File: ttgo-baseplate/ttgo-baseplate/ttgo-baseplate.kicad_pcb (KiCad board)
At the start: 4 copper layers, 55.1 x 76.6 mm, 4 parts, among them J1 Conn_02x16_Odd_Even, J2 Conn_02x16_Odd_Even, J3 Conn_02x10_Odd_Even, J4 Conn_01x05

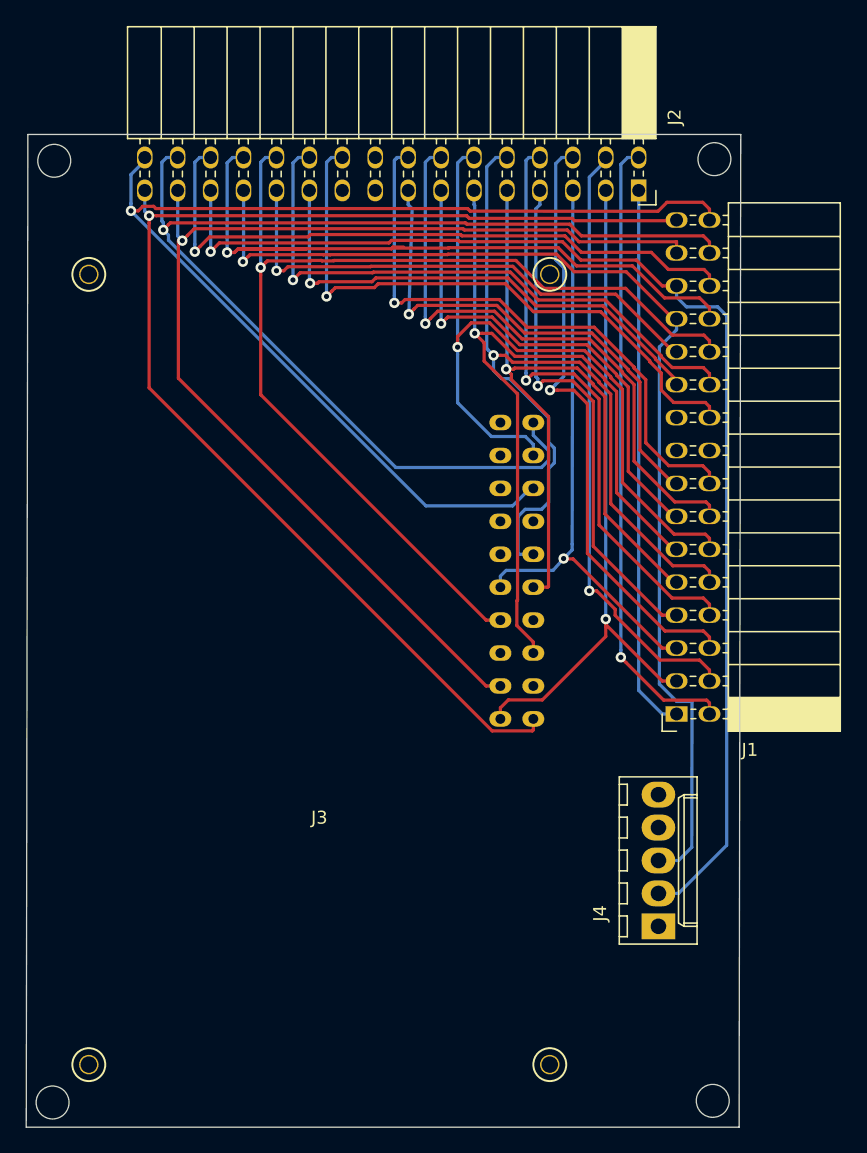
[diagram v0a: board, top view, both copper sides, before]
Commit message: texts added
new images for webpage
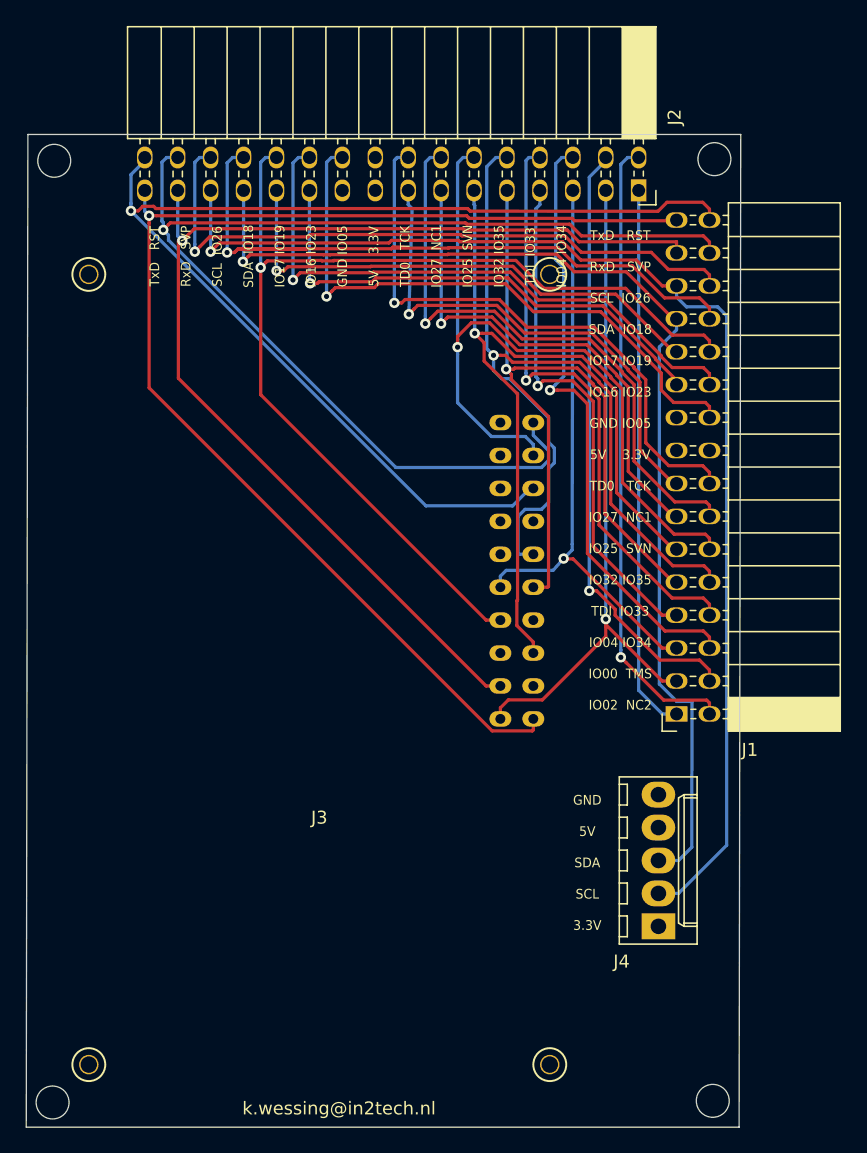
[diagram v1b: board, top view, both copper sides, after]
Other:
- board text added: "GND 5V SDA SCL 3.3V"
- board text added: "TTGO - BOARD Sensemakers - in2tech"
- board text added: "TxD RST RxD SVP SCL IO26 SDA IO18 IO17 IO19 IO16 IO23 GND IO05 5V 3.3V TD0 TCK IO27 NC1 IO25 SVN IO32 IO35 TDI IO33 IO04 IO34"
- board text added: "TxD RST RxD SVP SCL IO26 SDA IO18 IO17 IO19 IO16 IO23 GND IO05 5V 3.3V TD0 TCK IO27 NC1 IO25 SVN IO32 IO35 TDI IO33 IO04 IO34 IO00 TMS IO02 NC2"
- board text added: "k.wessing@in2tech.nl"
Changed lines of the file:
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@@
   (general
     (thickness 1.6)
-    (drawings 22)
+    (drawings 28)
     (tracks 538)
     (zones 0)
@@
     (descr "Connector Headers with Friction Lock, 22-27-2051, http://www.molex.com/pdm_docs/sd/022272021_sd.pdf")
     (tags "connector molex kk_6410 22-27-2051")
-    (fp_text reference J4 (at 1 -4.5 90) (layer F.SilkS)
+    (fp_text reference J4 (at -2.7178 -2.8448 180) (layer F.SilkS)
       (effects (font (size 1 1) (thickness 0.15)))
     )
@@
     )
   )
+  (gr_text "TTGO - BOARD\nSensemakers - in2tech" (at 138.0236 135.89) (layer B.SilkS)
+    (effects (font (size 1 1) (thickness 0.15)) (justify mirror))
+  )
+  (gr_text k.wessing@in2tech.nl (at 137.4648 142.2908) (layer B.SilkS)
+    (effects (font (size 1 1) (thickness 0.15)) (justify mirror))
+  )
+  (gr_text k.wessing@in2tech.nl (at 137.668 147.2692) (layer F.SilkS)
+    (effects (font (size 1 1) (thickness 0.15)))
+  )
+  (gr_text "GND\n\n5V\n\nSDA\n\nSCL\n\n3.3V" (at 156.8196 128.3208) (layer F.SilkS)
+    (effects (font (size 0.75 0.7) (thickness 0.15)))
+  )
+  (gr_text "TxD   RST\n                 \nRxD   SVP\n                 \nSCL  IO26\n                 \nSDA  IO18\n                 \nIO17 IO19\n                 \nIO16 IO23\n                 \nGND IO05\n                 \n5V    3.3V\n                 \nTD0   TCK\n                 \nIO27  NC1\n                 \nIO25  SVN\n                 \nIO32 IO35\n                 \nTDI  IO33\n                 \nIO04 IO34\n" (at 139.1412 81.534 90) (layer F.SilkS)
+    (effects (font (size 0.75 0.7) (thickness 0.15)))
+  )
+  (gr_text "TxD   RST\n                 \nRxD   SVP\n                 \nSCL  IO26\n                 \nSDA  IO18\n                 \nIO17 IO19\n                 \nIO16 IO23\n                 \nGND IO05\n                 \n5V    3.3V\n                 \nTD0   TCK\n                 \nIO27  NC1\n                 \nIO25  SVN\n                 \nIO32 IO35\n                 \nTDI  IO33\n                 \nIO04 IO34\n                 \nIO00  TMS\n                 \nIO02  NC2\n" (at 159.3596 98.044) (layer F.SilkS)
+    (effects (font (size 0.75 0.7) (thickness 0.15)))
+  )
   (dimension 6.477 (width 0.15) (layer Dwgs.User)
